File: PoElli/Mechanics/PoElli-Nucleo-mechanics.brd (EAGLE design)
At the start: 79.5 x 70 mm, 30 parts, among them J1 DF12-ELLI-HEADER-TOP, J3 M022.54MM, J4 M022.54MM, T1 Coilcraft 230NL, T2 FLYBACK750311689, U1 ENC424J600, X1 M-BOLT-2, X2 M-BOLT-2, X3 M-BOLT-2, X4 M-BOLT-2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

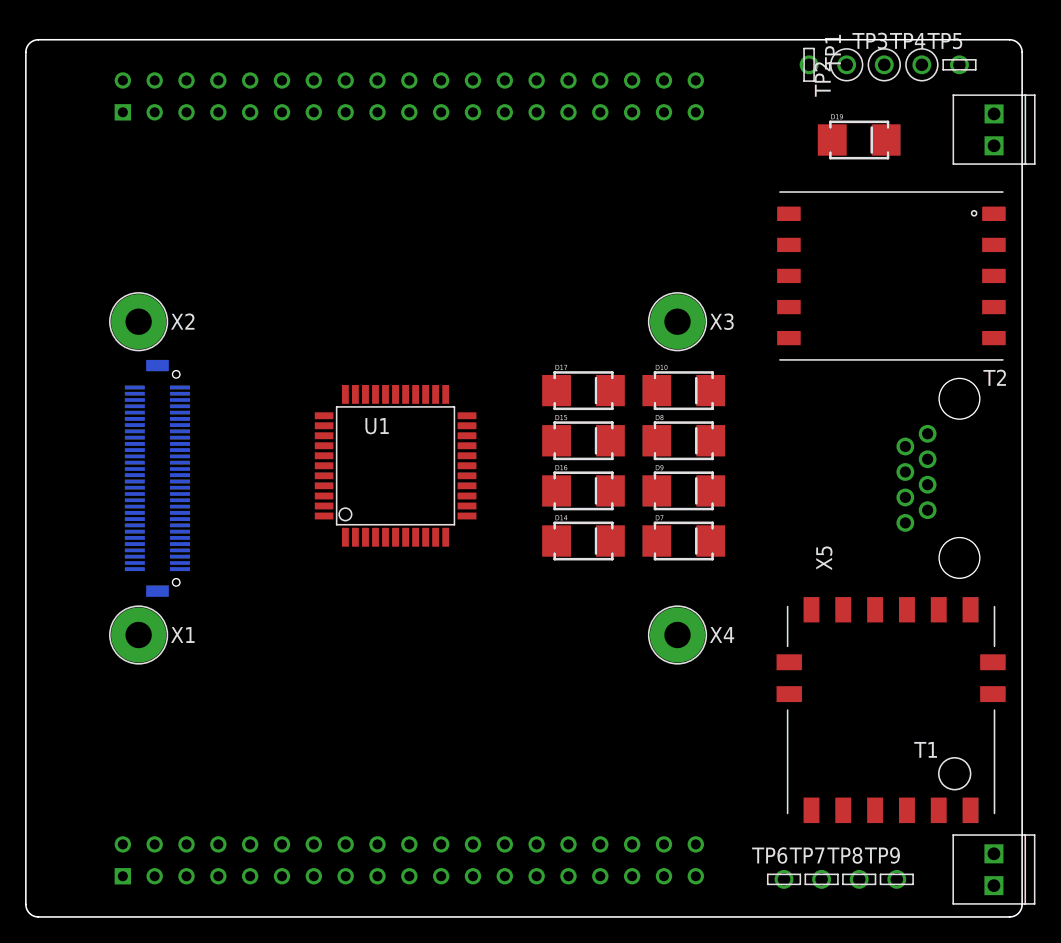
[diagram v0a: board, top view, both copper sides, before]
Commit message: Update PoElli/Mechanics non-produced boards with new library components
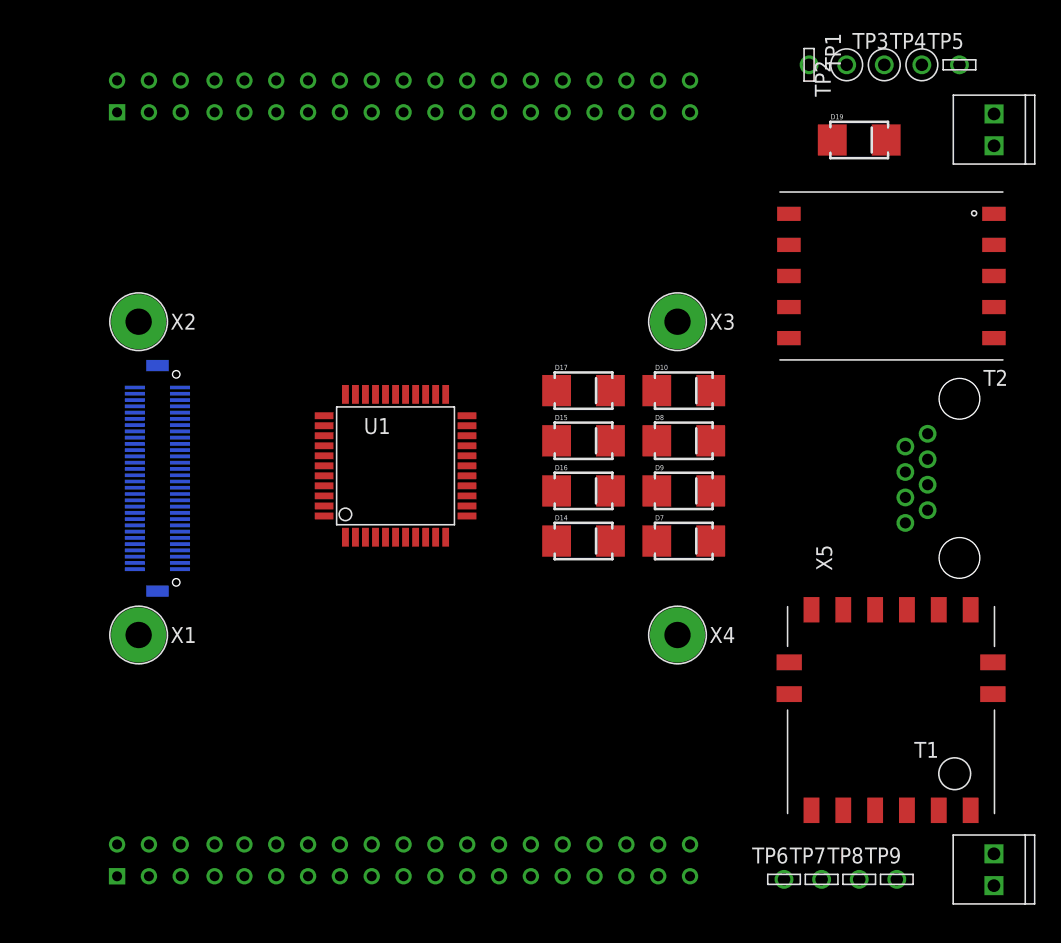
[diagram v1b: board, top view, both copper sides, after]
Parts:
- removed U$1: NUCLEO-SHIELD-UNDERSIDE-EXTENDED, ELL-i-Boards:NUCLEO-SHIELD-UNDERSIDE-EXTENDED
- added CN10: NUCLEO-CN10, ELL-i-Boards:NUCLEO-HEADER
- added CN7: NUCLEO-CN7, ELL-i-Boards:NUCLEO-HEADER
- added NUCLEO: NUCLEO-SHIELD-OUTLINE-EXTENDED, ELL-i-Boards:NUCLEO-SHIELD-UNDERSIDE-EXTENDED-OUTLINE
- renumbered J1 to EXT1
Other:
- board outline removed
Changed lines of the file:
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@@
 <layer number="47" name="Measures" color="7" fill="1" visible="no" active="yes"/>
 <layer number="48" name="Document" color="7" fill="1" visible="no" active="yes"/>
-<layer number="49" name="Reference" color="7" fill="1" visible="no" active="yes"/>
+<layer number="49" name="Reference" color="7" fill="1" visible="yes" active="yes"/>
 <layer number="50" name="dxf" color="7" fill="1" visible="no" active="no"/>
 <layer number="51" name="tDocu" color="7" fill="1" visible="yes" active="yes"/>
@@
 <layer number="220" name="220bmp" color="7" fill="1" visible="no" active="yes"/>
 <layer number="221" name="connection" color="7" fill="1" visible="no" active="yes"/>
+<layer number="222" name="222bmp" color="7" fill="1" visible="yes" active="yes"/>
 <layer number="223" name="223bmp" color="7" fill="1" visible="no" active="yes"/>
 <layer number="224" name="224bmp" color="7" fill="1" visible="no" active="yes"/>
@@
 <elements>
 <element name="T1" library="ELL-i-Transformers" package="COILCRAFT-ETH1-230L" value="Coilcraft 230NL" x="69.54" y="16.51" rot="R180"/>
-<element name="J1" library="ELL-i-Connectors" package="DF12(4.0)-60DP-0.5V" value="DF12-ELLI-HEADER-TOP" x="11" y="35" rot="MR90"/>
+<element name="EXT1" library="ELL-i-Connectors" package="DF12(4.0)-60DP-0.5V" value="DF12-ELLI-HEADER-TOP" x="11" y="35" rot="MR90"/>
 <element name="D17" library="ELL-i-DIscreteSemi" package="DIODE-B2100" value="B2100" x="45" y="42"/>
 <element name="D16" library="ELL-i-DIscreteSemi" package="DIODE-B2100" value="B2100" x="45" y="34"/>
@@
 <element name="X4" library="ELL-i-Connectors" package="M2-1" value="M-BOLT-2" x="52.5" y="22.5"/>
 <element name="X5" library="ELL-i-Connectors" package="MOLEX-43860-0001" value="POE-TP-RJ45-MOLEX" x="75" y="35" rot="R90"/>
-<element name="U$1" library="ELL-i-Boards" package="NUCLEO-SHIELD-UNDERSIDE-EXTENDED" value="NUCLEO-SHIELD-UNDERSIDE-EXTENDED" x="58" y="0" rot="R90"/>
 <element name="U1" library="ELL-i-DigitalIC" package="TQFP44-0.8MM" value="ENC424J600" x="30" y="36"/>
+<element name="NUCLEO" library="ELL-i-Boards" package="NUCLEO-SHIELD-UNDERSIDE-EXTENDED-OUTLINE" value="NUCLEO-SHIELD-OUTLINE-EXTENDED" x="0" y="0"/>
+<element name="CN7" library="ELL-i-Boards" package="NUCLEO-HEADER" value="NUCLEO-CN7" x="7.78" y="3.25"/>
+<element name="CN10" library="ELL-i-Boards" package="NUCLEO-HEADER" value="NUCLEO-CN10" x="7.78" y="64.21"/>
 </elements>
 <signals>
 <signal name="VIN">
-<contactref element="J1" pad="10"/>
+<contactref element="EXT1" pad="10"/>
 </signal>
 <signal name="VBATT">
-<contactref element="J1" pad="4"/>
+<contactref element="EXT1" pad="4"/>
 </signal>
 <signal name="N$1">
@@
 </signal>
 <signal name="5V">
-<contactref element="J1" pad="8"/>
+<contactref element="EXT1" pad="8"/>
 </signal>
 <signal name="POE_A+">
@@
 </signal>
 <signal name="VCC(IO)">
-<contactref element="J1" pad="2"/>
+<contactref element="EXT1" pad="2"/>
 </signal>
 <signal name="GND">
-<contactref element="J1" pad="14"/>
-<contactref element="J1" pad="12"/>
+<contactref element="EXT1" pad="14"/>
+<contactref element="EXT1" pad="12"/>
 <wire x1="12.8001" y1="30.25" x2="12.8001" y2="30.75" width="0" layer="19" extent="16-16"/>
 </signal>
 <signal name="3.3V">
-<contactref element="J1" pad="6"/>
+<contactref element="EXT1" pad="6"/>
 </signal>
 <signal name="N$13">

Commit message: Update Nucleo header origin to the center of the component
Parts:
- X5: value POE-TP-RJ45-MOLEX -> POE-TP-RJ45-MOLEX-43860-0001
- moved CN10 22.9 mm to (30.6, 65.5)
- moved CN7 22.9 mm to (30.6, 4.52)
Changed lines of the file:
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@@
 <layer number="111" name="111" color="7" fill="1" visible="no" active="yes"/>
 <layer number="112" name="tSilk" color="7" fill="1" visible="no" active="yes"/>
+<layer number="113" name="IDFDebug" color="4" fill="1" visible="yes" active="yes"/>
 <layer number="116" name="Patch_BOT" color="9" fill="4" visible="no" active="yes"/>
 <layer number="118" name="Rect_Pads" color="7" fill="1" visible="no" active="yes"/>
@@
 <element name="X3" library="ELL-i-Connectors" package="M2-1" value="M-BOLT-2" x="52.5" y="47.5"/>
 <element name="X4" library="ELL-i-Connectors" package="M2-1" value="M-BOLT-2" x="52.5" y="22.5"/>
-<element name="X5" library="ELL-i-Connectors" package="MOLEX-43860-0001" value="POE-TP-RJ45-MOLEX" x="75" y="35" rot="R90"/>
+<element name="X5" library="ELL-i-Connectors" package="MOLEX-43860-0001" value="POE-TP-RJ45-MOLEX-43860-0001" x="75" y="35" rot="R90"/>
 <element name="U1" library="ELL-i-DigitalIC" package="TQFP44-0.8MM" value="ENC424J600" x="30" y="36"/>
 <element name="NUCLEO" library="ELL-i-Boards" package="NUCLEO-SHIELD-UNDERSIDE-EXTENDED-OUTLINE" value="NUCLEO-SHIELD-OUTLINE-EXTENDED" x="0" y="0"/>
-<element name="CN7" library="ELL-i-Boards" package="NUCLEO-HEADER" value="NUCLEO-CN7" x="7.78" y="3.25"/>
-<element name="CN10" library="ELL-i-Boards" package="NUCLEO-HEADER" value="NUCLEO-CN10" x="7.78" y="64.21"/>
+<element name="CN7" library="ELL-i-Boards" package="NUCLEO-HEADER" value="NUCLEO-CN7" x="30.64" y="4.52"/>
+<element name="CN10" library="ELL-i-Boards" package="NUCLEO-HEADER" value="NUCLEO-CN10" x="30.64" y="65.48"/>
 </elements>
 <signals>
